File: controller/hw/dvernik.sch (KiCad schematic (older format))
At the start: 30 parts, among them P101 WAGO233, P102 CONN_01X06, P103 CONN_01X02, U101 A25L40P, U102 EK-TM4C123GXL, U103 Itead_HC-05, U104 LP2992AIM5-3.3CT-ND

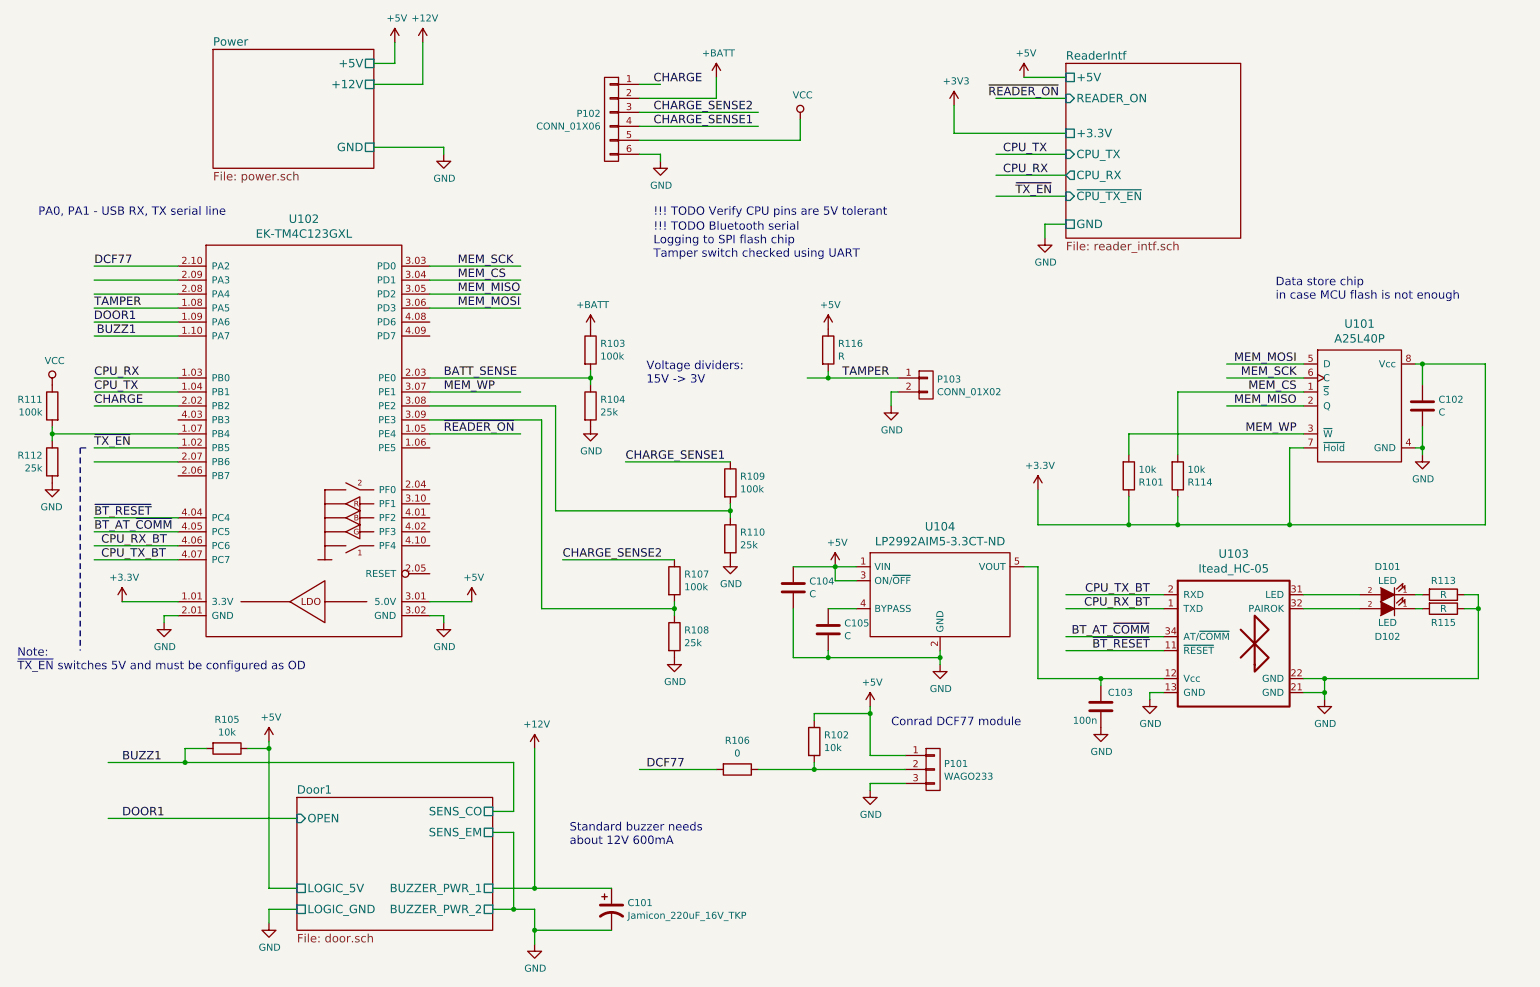
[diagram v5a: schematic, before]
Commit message: schematic improvements (door state pin for controller, fixes)
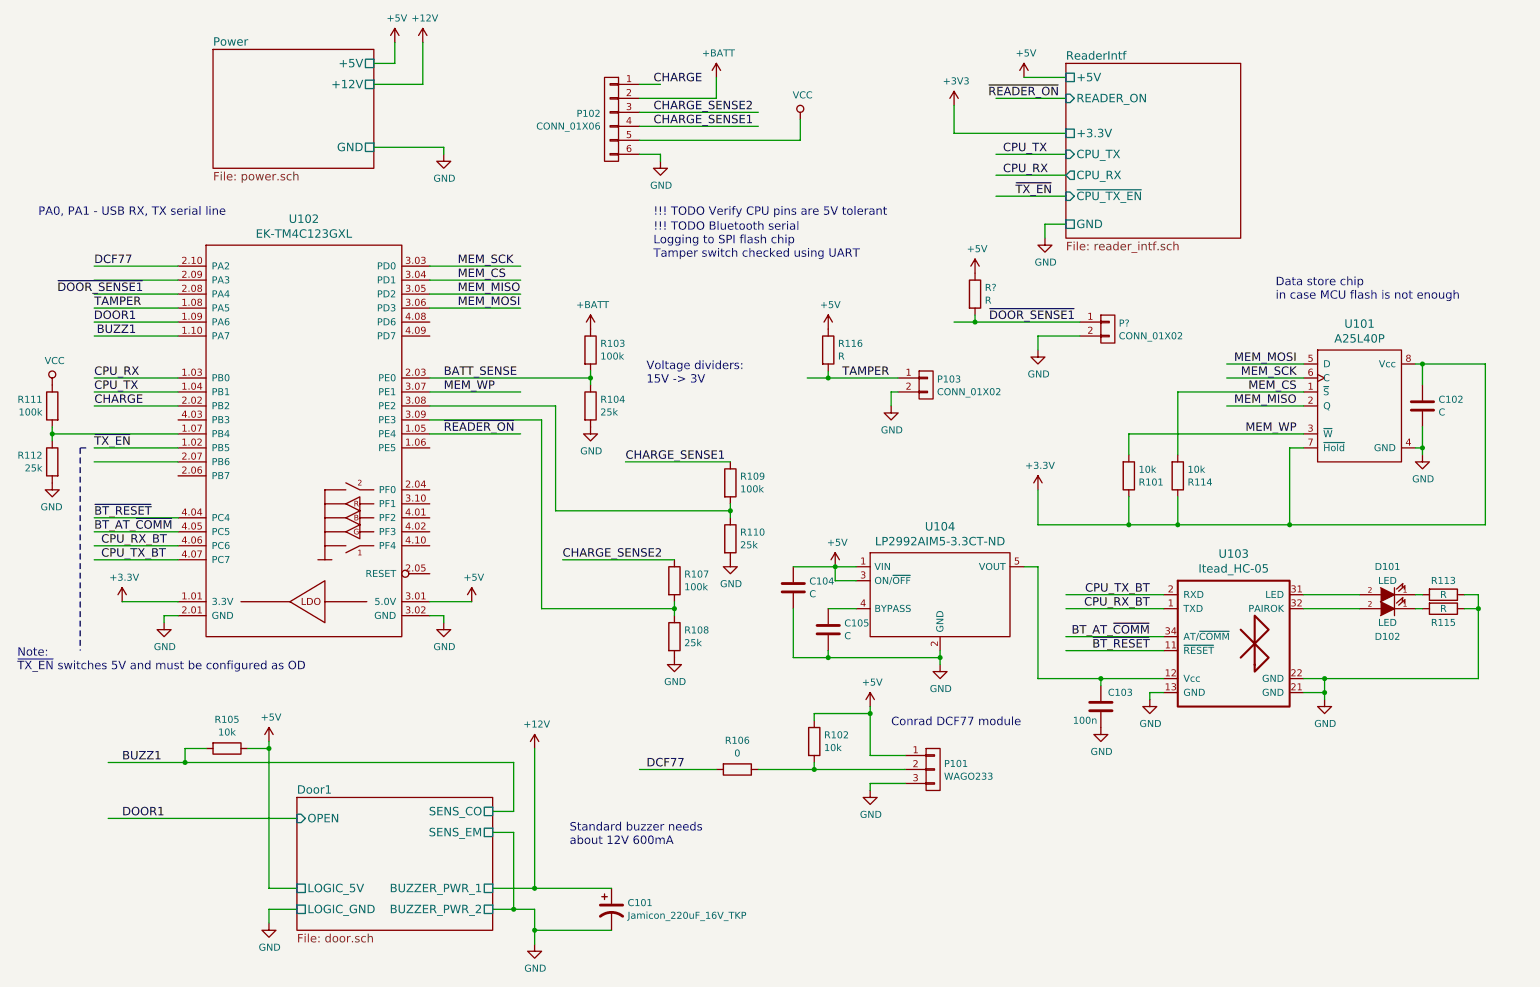
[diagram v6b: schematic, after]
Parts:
- added P?: CONN_01X02, th-npth:Wire-2_Wago-233-P2.5mm, symbol connectors:CONN_01X02
- added R?: R, smd-handsolder:R_1206_HandSoldering, symbol simple:R
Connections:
- net labels added: ~DOOR_SENSE1
- wire segments 142 -> 171
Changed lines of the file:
@@
 	11050 4250 11050 3100
 Wire Wire Line
-	7850 4250 11050 4250
+	7850 4250 8500 4250
 Connection ~ 6350 3200
 Wire Wire Line
@@
 	6800 3400 6800 3300
 Wire Wire Line
-	6850 3200 6200 3200
+	6850 3200 6350 3200
 Connection ~ 7150 5200
 Connection ~ 6350 5200
 Wire Wire Line
-	7150 5150 7150 5250
+	7150 5150 7150 5200
 Wire Wire Line
 	6350 5200 6350 5150
 Wire Wire Line
-	6100 5200 7150 5200
+	6100 5200 6350 5200
 Wire Wire Line
 	6100 4850 6100 5200
@@
 	6400 4550 6400 4650
 Wire Wire Line
-	6100 4550 6550 4550
+	6100 4550 6400 4550
 Wire Wire Line
 	6150 1500 6150 1350
@@
 	11000 4850 10900 4850
 Wire Wire Line
-	11000 4750 11000 5350
+	11000 4750 11000 4850
 Wire Wire Line
 	10900 4750 11000 4750
@@
 	9750 5450 9900 5450
 Wire Wire Line
-	9900 5350 9900 5500
-Wire Wire Line
-	11000 5350 9750 5350
-Wire Wire Line
-	7850 5350 8750 5350
+	9900 5350 9900 5450
+Wire Wire Line
+	11000 5350 9900 5350
+Wire Wire Line
+	7850 5350 8300 5350
 Connection ~ 800  3600
 Wire Wire Line
-	800  3550 800  3650
+	800  3550 800  3600
 Wire Wire Line
 	800  3600 1700 3600
@@
 Connection ~ 5250 4850
 Wire Wire Line
-	5250 4800 5250 4900
+	5250 4800 5250 4850
 Connection ~ 5650 4150
 Wire Wire Line
-	5650 4100 5650 4200
+	5650 4100 5650 4150
 Wire Wire Line
 	4400 4150 5650 4150
@@
 	2200 5850 2350 5850
 Wire Wire Line
-	4100 5950 1200 5950
+	4100 5950 1750 5950
 Wire Wire Line
 	4100 6300 4100 5950
@@
 	2350 7100 2350 7000
 Wire Wire Line
-	2350 5800 2350 6850
+	2350 5800 2350 5850
 Wire Wire Line
 	4250 7150 4800 7150
 Wire Wire Line
-	3950 7000 4250 7000
-Wire Wire Line
-	4250 7000 4250 7250
+	3950 7000 4100 7000
+Wire Wire Line
+	4250 7000 4250 7150
 Wire Wire Line
 	4250 6850 4250 5850
@@
 	6250 5950 6250 6000
 Wire Wire Line
-	6650 5550 6650 5900
+	6650 5550 6650 5600
 Wire Wire Line
 	6650 6150 6650 6100
@@
 	6650 5900 6900 5900
 Wire Wire Line
-	5850 6000 6900 6000
+	5850 6000 6250 6000
 Wire Wire Line
 	3250 800  3250 950
@@
 Connection ~ 4250 6850
 Wire Wire Line
-	3950 6850 4800 6850
+	3950 6850 4250 6850
 Wire Wire Line
 	1700 3700 1100 3700
@@
 Connection ~ 10600 3700
 Wire Wire Line
-	10600 3550 10600 3750
+	10600 3550 10600 3700
 Connection ~ 10600 3100
 Wire Wire Line
 	10550 3700 10600 3700
 Wire Wire Line
-	10550 3100 11050 3100
+	10550 3100 10600 3100
 Wire Wire Line
 	9750 3700 9650 3700
@@
 Connection ~ 4650 3200
 Wire Wire Line
-	4650 3150 4650 3250
+	4650 3150 4650 3200
 Wire Wire Line
 	3500 3200 4650 3200
@@
 Wire Wire Line
 	3500 2400 4150 2400
+Wire Wire Line
+	8850 4250 9650 4250
+Wire Wire Line
+	8500 4250 8850 4250
+Wire Wire Line
+	9650 4250 11050 4250
+Wire Wire Line
+	6350 3200 6200 3200
+Wire Wire Line
+	7150 5200 7150 5250
+Wire Wire Line
+	6350 5200 7150 5200
+Wire Wire Line
+	6400 4550 6550 4550
+Wire Wire Line
+	11000 4850 11000 5350
+Wire Wire Line
+	9900 5350 9750 5350
+Wire Wire Line
+	8300 5350 8750 5350
+Wire Wire Line
+	9900 5450 9900 5500
+Wire Wire Line
+	800  3600 800  3650
+Wire Wire Line
+	5250 4850 5250 4900
+Wire Wire Line
+	5650 4150 5650 4200
+Wire Wire Line
+	1750 5950 1200 5950
+Wire Wire Line
+	2350 5850 2350 6850
+Wire Wire Line
+	4100 7000 4250 7000
+Wire Wire Line
+	6650 5600 6650 5900
+Wire Wire Line
+	6250 6000 6900 6000
+Wire Wire Line
+	4250 7150 4250 7250
+Wire Wire Line
+	4250 6850 4800 6850
+Wire Wire Line
+	10600 3700 10600 3750
+Wire Wire Line
+	10600 3100 11050 3100
+Wire Wire Line
+	4650 3200 4650 3250
+$Comp
+L connectors:CONN_01X02 P?
+U 1 1 5A3A3764
+P 8350 2850
+F 0 "P?" H 8428 2891 50  0000 L CNN
+F 1 "CONN_01X02" H 8428 2800 50  0000 L CNN
+F 2 "th-npth:Wire-2_Wago-233-P2.5mm" H 8350 2850 60  0001 C CNN
+F 3 "" H 8350 2850 60  0000 C CNN
+	1    8350 2850
+	1    0    0    -1
+$EndComp
+$Comp
+L mspower:GND #PWR?
+U 1 1 5A3A376A
+P 7850 3000
+F 0 "#PWR?" H 7850 2750 50  0001 C CNN
+F 1 "GND" H 7855 2827 50  0000 C CNN
+F 2 "" H 7850 3000 60  0000 C CNN
+F 3 "" H 7850 3000 60  0000 C CNN
+	1    7850 3000
+	1    0    0    -1
+$EndComp
+Text Label 7500 2800 0    60   ~ 0
+~DOOR_SENSE1
+$Comp
+L simple:R R?
+U 1 1 5A3A3771
+P 7400 2600
+F 0 "R?" H 7470 2646 50  0000 L CNN
+F 1 "R" H 7470 2555 50  0000 L CNN
+F 2 "smd-handsolder:R_1206_HandSoldering" V 7330 2600 30  0001 C CNN
+F 3 "" H 7400 2600 30  0000 C CNN
+	1    7400 2600
+	1    0    0    -1
+$EndComp
+$Comp
+L mspower:+5V #PWR?
+U 1 1 5A3A3777
+P 7400 2450
+F 0 "#PWR?" H 7400 2300 50  0001 C CNN
+F 1 "+5V" H 7415 2623 50  0000 C CNN
+F 2 "" H 7400 2450 60  0000 C CNN
+F 3 "" H 7400 2450 60  0000 C CNN
+	1    7400 2450
+	1    0    0    -1
+$EndComp
+Connection ~ 7400 2800
+Wire Wire Line
+	7400 2750 7400 2800
+Wire Wire Line
+	7850 2900 8150 2900
+Wire Wire Line
+	7850 3000 7850 2900
+Wire Wire Line
+	8150 2800 7400 2800
+Wire Wire Line
+	7400 2800 7250 2800
+Text Label 1450 2600 2    60   ~ 0
+~DOOR_SENSE1
 $EndSCHEMATC
